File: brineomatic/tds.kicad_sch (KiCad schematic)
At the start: 4 parts, among them J15 TDS

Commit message: starting to shape up, footprints etc
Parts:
- J14: renamed from J15; footprint (none) -> TerminalBlock_Phoenix:TerminalBlock_Phoenix_PT-1,5-3-3.5-H_1x03_P3.50mm_Horizontal
- renumbered R38 to R35
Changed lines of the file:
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@@
 		(dnp no)
 		(fields_autoplaced yes)
-		(property "Reference" "J15"
+		(property "Reference" "J14"
 			(at 92.71 76.2 0)
 			(effects
@@
 			)
 		)
-		(property "Footprint" ""
+		(property "Footprint" "TerminalBlock_Phoenix:TerminalBlock_Phoenix_PT-1,5-3-3.5-H_1x03_P3.50mm_Horizontal"
 			(at 92.71 85.09 0)
 			(effects
@@
 			(project ""
 				(path "/96477ae2-ef08-48f3-8dd4-fe4478541f68/4dde40bf-0b86-4621-acd9-eb6c6b71c357"
-					(reference "J15")
+					(reference "J14")
 					(unit 1)
 				)
@@
 		(dnp no)
 		(fields_autoplaced yes)
-		(property "Reference" "#PWR044"
+		(property "Reference" "#PWR041"
 			(at 101.6 77.47 0)
 			(effects
@@
 			(project "brineomatic"
 				(path "/96477ae2-ef08-48f3-8dd4-fe4478541f68/4dde40bf-0b86-4621-acd9-eb6c6b71c357"
-					(reference "#PWR044")
+					(reference "#PWR041")
 					(unit 1)
 				)
@@
 		(dnp no)
 		(fields_autoplaced yes)
-		(property "Reference" "R38"
+		(property "Reference" "R35"
 			(at 124.46 78.74 90)
 			(effects
@@
 			(project "brineomatic"
 				(path "/96477ae2-ef08-48f3-8dd4-fe4478541f68/4dde40bf-0b86-4621-acd9-eb6c6b71c357"
-					(reference "R38")
+					(reference "R35")
 					(unit 1)
 				)
@@
 		(dnp no)
 		(fields_autoplaced yes)
-		(property "Reference" "#PWR043"
+		(property "Reference" "#PWR042"
 			(at 101.6 104.14 0)
 			(effects
@@
 			(project "brineomatic"
 				(path "/96477ae2-ef08-48f3-8dd4-fe4478541f68/4dde40bf-0b86-4621-acd9-eb6c6b71c357"
-					(reference "#PWR043")
-					(unit 1)
-				)
+					(reference "#PWR042")
+					(unit 1)
+				)

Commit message: starting to look good.
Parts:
- J14: footprint TerminalBlock_Phoenix:TerminalBlock_Phoenix_PT-1,5-3-3.5-H_1x03_P3.50mm_Horizontal -> Connector_JST:JST_PH_S3B-PH-K_1x03_P2.00mm_Horizontal
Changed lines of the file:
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@@
 			)
 		)
-		(property "Footprint" "TerminalBlock_Phoenix:TerminalBlock_Phoenix_PT-1,5-3-3.5-H_1x03_P3.50mm_Horizontal"
+		(property "Footprint" "Connector_JST:JST_PH_S3B-PH-K_1x03_P2.00mm_Horizontal"
 			(at 92.71 85.09 0)
 			(effects

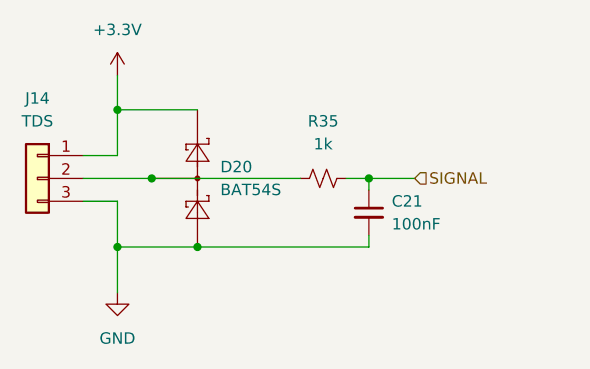
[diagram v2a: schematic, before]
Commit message: updated bom and prepping for Rev A
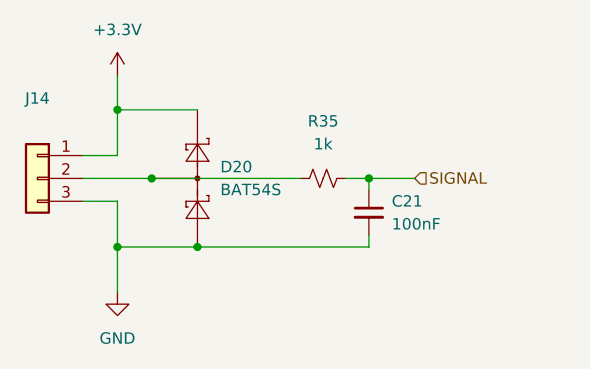
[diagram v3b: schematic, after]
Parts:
- J14: value TDS -> ~; LCSC (none) -> C157929
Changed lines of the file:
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@@
 			)
 		)
-		(property "Value" "TDS"
+		(property "Value" "~"
 			(at 92.71 78.74 0)
 			(effects
@@
 			(at 92.71 85.09 0)
 			(effects
+				(font
+					(size 1.27 1.27)
+				)
+				(hide yes)
+			)
+		)
+		(property "LCSC" "C157929"
+			(at 92.71 85.09 0)
+			(effects

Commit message: fixed bat54s placement.
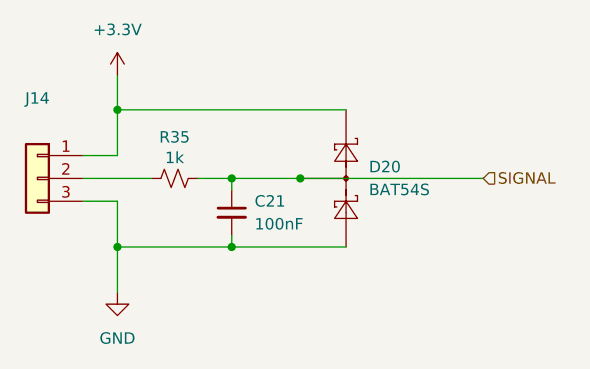
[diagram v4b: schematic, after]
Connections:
- net SIGNAL: now also D20.3 (COM)
- net at J14.2 (Pin_2), R35.1: no longer D20.3 (COM)
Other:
- moved on the sheet: C21, D20, R35
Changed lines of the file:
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@@
 	(paper "A4")
+	(junction
+		(at 114.3 92.71)
+		(diameter 0)
+		(color 0 0 0 0)
+	)
+	(junction
+		(at 114.3 85.09)
+		(diameter 0)
+		(color 0 0 0 0)
+	)
+	(junction
+		(at 121.92 85.09)
+		(diameter 0)
+		(color 0 0 0 0)
+	)
 	(junction
 		(at 101.6 77.47)
@@
 	)
 	(junction
-		(at 129.54 85.09)
-		(diameter 0)
-		(color 0 0 0 0)
-	)
-	(junction
-		(at 110.49 92.71)
-		(diameter 0)
-		(color 0 0 0 0)
-	)
-	(junction
-		(at 105.41 85.09)
-		(diameter 0)
-		(color 0 0 0 0)
-	)
-	(junction
 		(at 101.6 92.71)
 		(diameter 0)
@@
 	(wire
 		(pts
-			(xy 127 85.09) (xy 129.54 85.09)
-		)
-		(stroke
-			(width 0)
-			(type default)
-		)
-	)
-	(wire
-		(pts
-			(xy 129.54 85.09) (xy 134.62 85.09)
+			(xy 110.49 85.09) (xy 114.3 85.09)
 		)
 		(stroke
@@
 	(wire
 		(pts
+			(xy 121.92 85.09) (xy 142.24 85.09)
+		)
+		(stroke
+			(width 0)
+			(type default)
+		)
+	)
+	(wire
+		(pts
+			(xy 101.6 77.47) (xy 127 77.47)
+		)
+		(stroke
+			(width 0)
+			(type default)
+		)
+	)
+	(wire
+		(pts
+			(xy 114.3 91.44) (xy 114.3 92.71)
+		)
+		(stroke
+			(width 0)
+			(type default)
+		)
+	)
+	(wire
+		(pts
+			(xy 114.3 92.71) (xy 127 92.71)
+		)
+		(stroke
+			(width 0)
+			(type default)
+		)
+	)
+	(wire
+		(pts
 			(xy 97.79 85.09) (xy 105.41 85.09)
 		)
@@
 	(wire
 		(pts
-			(xy 101.6 77.47) (xy 110.49 77.47)
-		)
-		(stroke
-			(width 0)
-			(type default)
-		)
-	)
-	(wire
-		(pts
-			(xy 129.54 85.09) (xy 129.54 86.36)
-		)
-		(stroke
-			(width 0)
-			(type default)
-		)
-	)
-	(wire
-		(pts
-			(xy 129.54 91.44) (xy 129.54 92.71)
-		)
-		(stroke
-			(width 0)
-			(type default)
-		)
-	)
-	(wire
-		(pts
-			(xy 110.49 92.71) (xy 129.54 92.71)
-		)
-		(stroke
-			(width 0)
-			(type default)
-		)
-	)
-	(wire
-		(pts
 			(xy 101.6 73.66) (xy 101.6 77.47)
 		)
@@
 	(wire
 		(pts
-			(xy 105.41 85.09) (xy 121.92 85.09)
-		)
-		(stroke
-			(width 0)
-			(type default)
-		)
-	)
-	(wire
-		(pts
-			(xy 101.6 92.71) (xy 110.49 92.71)
+			(xy 114.3 85.09) (xy 114.3 86.36)
+		)
+		(stroke
+			(width 0)
+			(type default)
+		)
+	)
+	(wire
+		(pts
+			(xy 114.3 85.09) (xy 121.92 85.09)
+		)
+		(stroke
+			(width 0)
+			(type default)
+		)
+	)
+	(wire
+		(pts
+			(xy 101.6 92.71) (xy 114.3 92.71)
 		)
 		(stroke
@@
 	(hierarchical_label "SIGNAL"
 		(shape input)
-		(at 134.62 85.09 0)
+		(at 142.24 85.09 0)
 		(fields_autoplaced yes)
 		(effects
@@
 	(symbol
 		(lib_id "Device:R_Small_US")
-		(at 124.46 85.09 90)
+		(at 107.95 85.09 90)
 		(unit 1)
 		(exclude_from_sim no)
@@
 		(on_board yes)
 		(dnp no)
-		(fields_autoplaced yes)
 		(property "Reference" "R35"
-			(at 124.46 78.74 90)
+			(at 107.95 80.518 90)
 			(effects
 				(font
@@
 		)
 		(property "Value" "1k"
-			(at 124.46 81.28 90)
+			(at 107.95 82.804 90)
 			(effects
 				(font
@@
 		)
 		(property "Footprint" "Resistor_SMD:R_0805_2012Metric_Pad1.20x1.40mm_HandSolder"
-			(at 124.46 85.09 0)
+			(at 107.95 85.09 0)
 			(effects
 				(font
@@
 		)
 		(property "Datasheet" "~"
-			(at 124.46 85.09 0)
+			(at 107.95 85.09 0)
 			(effects
 				(font
@@
 		)
 		(property "Description" ""
-			(at 124.46 85.09 0)
+			(at 107.95 85.09 0)
 			(effects
 				(font
@@
 		)
 		(property "LCSC" "C95781"
-			(at 124.46 85.09 0)
+			(at 107.95 85.09 0)
 			(effects
 				(font
@@
 	(symbol
 		(lib_id "Device:C_Small")
-		(at 129.54 88.9 0)
+		(at 114.3 88.9 0)
 		(unit 1)
 		(exclude_from_sim no)
@@
 		(dnp no)
 		(property "Reference" "C21"
-			(at 132.08 87.6363 0)
+			(at 116.84 87.6363 0)
 			(effects
 				(font
@@
 		)
 		(property "Value" "100nF"
-			(at 132.08 90.1763 0)
+			(at 116.84 90.1763 0)
 			(effects
 				(font
@@
 		)
 		(property "Footprint" "Capacitor_SMD:C_0805_2012Metric_Pad1.18x1.45mm_HandSolder"
-			(at 129.54 88.9 0)
+			(at 114.3 88.9 0)
 			(effects
 				(font
@@
 		)
 		(property "Datasheet" "~"
-			(at 129.54 88.9 0)
+			(at 114.3 88.9 0)
 			(effects
 				(font
@@
 		)
 		(property "Description" ""
-			(at 129.54 88.9 0)
+			(at 114.3 88.9 0)
 			(effects
 				(font
@@
 		)
 		(property "Mouser" ""
-			(at 129.54 88.9 0)
+			(at 114.3 88.9 0)
 			(effects
 				(font
@@
 		)
 		(property "LCSC" "C49678"
-			(at 129.54 88.9 0)
+			(at 114.3 88.9 0)
 			(effects
 				(font
@@
 	(symbol
 		(lib_id "Diode:BAT54S")
-		(at 110.49 85.09 270)
+		(at 127 85.09 270)
 		(mirror x)
 		(unit 1)
@@
 		(fields_autoplaced yes)
 		(property "Reference" "D20"
-			(at 113.03 83.82 90)
+			(at 129.54 83.82 90)
 			(effects
 				(font
@@
 		)
 		(property "Value" "BAT54S"
-			(at 113.03 86.36 90)
+			(at 129.54 86.36 90)
 			(effects
 				(font
@@
 		)
 		(property "Footprint" "Package_TO_SOT_SMD:SOT-23"
-			(at 113.665 83.185 0)
+			(at 130.175 83.185 0)
 			(effects
 				(font
@@
 		)
 		(property "Datasheet" "https://www.diodes.com/assets/Datasheets/ds11005.pdf"
-			(at 110.49 88.138 0)
+			(at 127 88.138 0)
 			(effects
 				(font
@@
 		)
 		(property "Description" ""
-			(at 110.49 85.09 0)
+			(at 127 85.09 0)
 			(effects
 				(font
@@
 		)
 		(property "LCSC" "C727126"
-			(at 110.49 85.09 90)
-			(effects
-				(font
+			(at 127 85.09 90)
+			(effects
+				(font

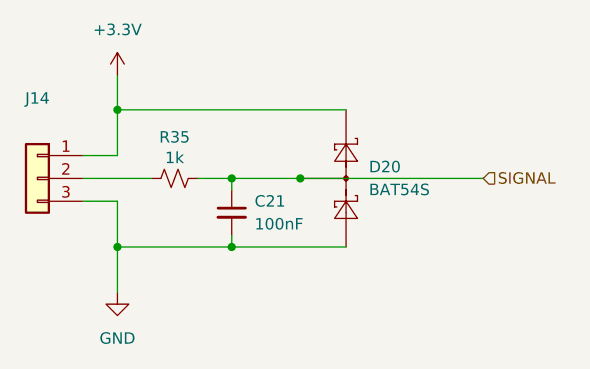
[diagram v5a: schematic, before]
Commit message: did a bunch of schematic work for Rev B
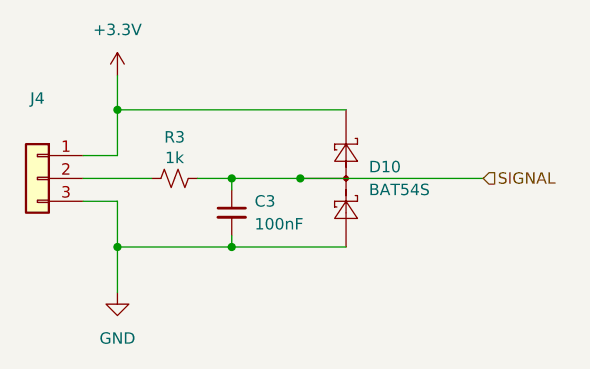
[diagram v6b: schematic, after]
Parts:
- renumbered C21 to C3, D20 to D10, J14 to J4, R35 to R3
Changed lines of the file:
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@@
 		(dnp no)
 		(fields_autoplaced yes)
-		(property "Reference" "J14"
+		(property "Reference" "J4"
 			(at 92.71 76.2 0)
 			(effects
@@
 		)
 		(instances
-			(project ""
-				(path "/96477ae2-ef08-48f3-8dd4-fe4478541f68/4dde40bf-0b86-4621-acd9-eb6c6b71c357"
-					(reference "J14")
+			(project "brineomatic"
+				(path "/96477ae2-ef08-48f3-8dd4-fe4478541f68/be3403ab-9eef-436c-86e7-0de3f072ae30"
+					(reference "J4")
 					(unit 1)
 				)
@@
 		(dnp no)
 		(fields_autoplaced yes)
-		(property "Reference" "#PWR041"
+		(property "Reference" "#PWR013"
 			(at 101.6 77.47 0)
 			(effects
@@
 				(path "/96477ae2-ef08-48f3-8dd4-fe4478541f68/4dde40bf-0b86-4621-acd9-eb6c6b71c357"
 					(reference "#PWR041")
+					(unit 1)
+				)
+				(path "/96477ae2-ef08-48f3-8dd4-fe4478541f68/be3403ab-9eef-436c-86e7-0de3f072ae30"
+					(reference "#PWR013")
 					(unit 1)
 				)
@@
 		(on_board yes)
 		(dnp no)
-		(property "Reference" "R35"
+		(property "Reference" "R3"
 			(at 107.95 80.518 90)
 			(effects
@@
 				(path "/96477ae2-ef08-48f3-8dd4-fe4478541f68/4dde40bf-0b86-4621-acd9-eb6c6b71c357"
 					(reference "R35")
+					(unit 1)
+				)
+				(path "/96477ae2-ef08-48f3-8dd4-fe4478541f68/be3403ab-9eef-436c-86e7-0de3f072ae30"
+					(reference "R3")
 					(unit 1)
 				)
@@
 		(dnp no)
 		(fields_autoplaced yes)
-		(property "Reference" "#PWR042"
+		(property "Reference" "#PWR014"
 			(at 101.6 104.14 0)
 			(effects
@@
 				(path "/96477ae2-ef08-48f3-8dd4-fe4478541f68/4dde40bf-0b86-4621-acd9-eb6c6b71c357"
 					(reference "#PWR042")
+					(unit 1)
+				)
+				(path "/96477ae2-ef08-48f3-8dd4-fe4478541f68/be3403ab-9eef-436c-86e7-0de3f072ae30"
+					(reference "#PWR014")
 					(unit 1)
 				)
@@
 		(on_board yes)
 		(dnp no)
-		(property "Reference" "C21"
+		(property "Reference" "C3"
 			(at 116.84 87.6363 0)
 			(effects
@@
 				(path "/96477ae2-ef08-48f3-8dd4-fe4478541f68/4dde40bf-0b86-4621-acd9-eb6c6b71c357"
 					(reference "C21")
+					(unit 1)
+				)
+				(path "/96477ae2-ef08-48f3-8dd4-fe4478541f68/be3403ab-9eef-436c-86e7-0de3f072ae30"
+					(reference "C3")
 					(unit 1)
 				)
@@
 		(dnp no)
 		(fields_autoplaced yes)
-		(property "Reference" "D20"
+		(property "Reference" "D10"
 			(at 129.54 83.82 90)
 			(effects
@@
 					(unit 1)
 				)
+				(path "/96477ae2-ef08-48f3-8dd4-fe4478541f68/be3403ab-9eef-436c-86e7-0de3f072ae30"
+					(reference "D10")
+					(unit 1)
+				)

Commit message: worked on schematic and layout a bit more.
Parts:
- C3: footprint Capacitor_SMD:C_0805_2012Metric_Pad1.18x1.45mm_HandSolder -> Capacitor_SMD:C_0603_1608Metric
- R3: footprint Resistor_SMD:R_0805_2012Metric_Pad1.20x1.40mm_HandSolder -> Resistor_SMD:R_0603_1608Metric
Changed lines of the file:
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@@
 		(instances
 			(project "brineomatic"
+				(path "/96477ae2-ef08-48f3-8dd4-fe4478541f68/4dde40bf-0b86-4621-acd9-eb6c6b71c357"
+					(reference "J14")
+					(unit 1)
+				)
 				(path "/96477ae2-ef08-48f3-8dd4-fe4478541f68/be3403ab-9eef-436c-86e7-0de3f072ae30"
 					(reference "J4")
@@
 			)
 		)
-		(property "Footprint" "Resistor_SMD:R_0805_2012Metric_Pad1.20x1.40mm_HandSolder"
+		(property "Footprint" "Resistor_SMD:R_0603_1608Metric"
 			(at 107.95 85.09 0)
 			(effects
@@
 			)
 		)
-		(property "Footprint" "Capacitor_SMD:C_0805_2012Metric_Pad1.18x1.45mm_HandSolder"
+		(property "Footprint" "Capacitor_SMD:C_0603_1608Metric"
 			(at 114.3 88.9 0)
 			(effects

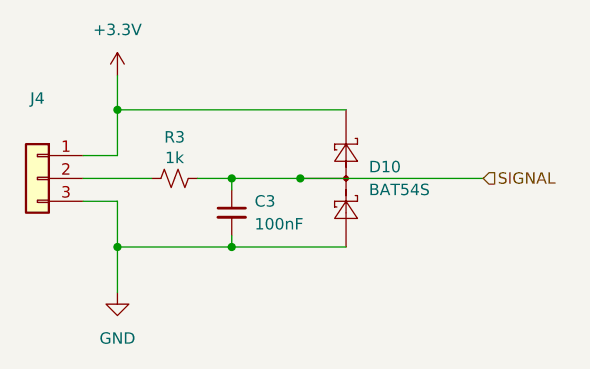
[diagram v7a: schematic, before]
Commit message: updated wiring and connector to match dfrobot for tds sensors
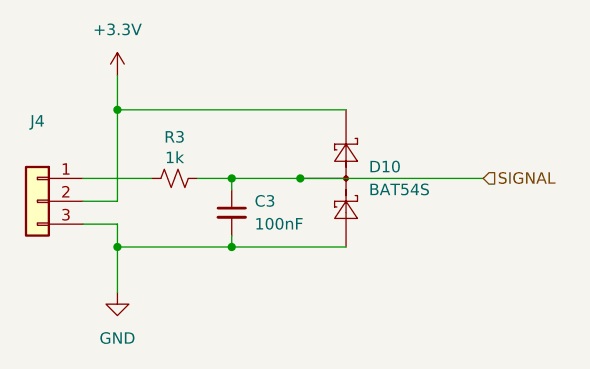
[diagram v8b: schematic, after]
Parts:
- J4: footprint Connector_JST:JST_PH_S3B-PH-K_1x03_P2.00mm_Horizontal -> Connector_PinHeader_2.54mm:PinHeader_1x03_P2.54mm_Horizontal; LCSC C157929 -> (none)
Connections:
- net +3.3V: now also J4.2 (Pin_2); no longer J4.1 (Pin_1)
- net at R3.1: now also J4.1 (Pin_1); no longer J4.2 (Pin_2)
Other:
- moved on the sheet: J4
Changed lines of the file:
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@@
 	(wire
 		(pts
-			(xy 101.6 77.47) (xy 101.6 82.55)
-		)
-		(stroke
-			(width 0)
-			(type default)
-		)
-	)
-	(wire
-		(pts
-			(xy 101.6 87.63) (xy 101.6 92.71)
+			(xy 101.6 77.47) (xy 101.6 87.63)
+		)
+		(stroke
+			(width 0)
+			(type default)
+		)
+	)
+	(wire
+		(pts
+			(xy 101.6 87.63) (xy 97.79 87.63)
+		)
+		(stroke
+			(width 0)
+			(type default)
+		)
+	)
+	(wire
+		(pts
+			(xy 101.6 90.17) (xy 101.6 92.71)
+		)
+		(stroke
+			(width 0)
+			(type default)
+		)
+	)
+	(wire
+		(pts
+			(xy 97.79 85.09) (xy 105.41 85.09)
 		)
 		(stroke
@@
 	(wire
 		(pts
-			(xy 97.79 82.55) (xy 101.6 82.55)
-		)
-		(stroke
-			(width 0)
-			(type default)
-		)
-	)
-	(wire
-		(pts
 			(xy 121.92 85.09) (xy 142.24 85.09)
 		)
@@
 	(wire
 		(pts
-			(xy 97.79 85.09) (xy 105.41 85.09)
-		)
-		(stroke
-			(width 0)
-			(type default)
-		)
-	)
-	(wire
-		(pts
 			(xy 101.6 73.66) (xy 101.6 77.47)
 		)
@@
 	(wire
 		(pts
-			(xy 97.79 87.63) (xy 101.6 87.63)
+			(xy 97.79 90.17) (xy 101.6 90.17)
 		)
 		(stroke
@@
 	(symbol
 		(lib_id "Connector_Generic:Conn_01x03")
-		(at 92.71 85.09 0)
+		(at 92.71 87.63 0)
 		(mirror y)
 		(unit 1)
@@
 		(fields_autoplaced yes)
 		(property "Reference" "J4"
-			(at 92.71 76.2 0)
+			(at 92.71 78.74 0)
 			(effects
 				(font
@@
 		)
 		(property "Value" "~"
-			(at 92.71 78.74 0)
-			(effects
-				(font
-					(size 1.27 1.27)
-				)
-			)
-		)
-		(property "Footprint" "Connector_JST:JST_PH_S3B-PH-K_1x03_P2.00mm_Horizontal"
-			(at 92.71 85.09 0)
+			(at 92.71 81.28 0)
+			(effects
+				(font
+					(size 1.27 1.27)
+				)
+			)
+		)
+		(property "Footprint" "Connector_PinHeader_2.54mm:PinHeader_1x03_P2.54mm_Horizontal"
+			(at 92.71 87.63 0)
 			(effects
 				(font
@@
 		)
 		(property "Datasheet" "~"
-			(at 92.71 85.09 0)
+			(at 92.71 87.63 0)
 			(effects
 				(font
@@
 		)
 		(property "Description" "Generic connector, single row, 01x03, script generated (kicad-library-utils/schlib/autogen/connector/)"
-			(at 92.71 85.09 0)
+			(at 92.71 87.63 0)
 			(effects
 				(font
@@
 			)
 		)
-		(property "LCSC" "C157929"
-			(at 92.71 85.09 0)
-			(effects
-				(font
+		(property "LCSC" ""
+			(at 92.71 87.63 0)
+			(effects
+				(font
